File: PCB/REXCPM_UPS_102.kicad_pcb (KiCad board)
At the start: 2 copper layers, 60 x 16 mm, 9 parts, among them J2 SM04B, J3 Conn_02x20_Odd_Even, U1 742G02

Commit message: remove all mention of model 200, since REXCPM does not support it
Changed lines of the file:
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@@
   (paper "USLetter")
   (title_block
-    (title "REXCPM_UPS_102_200")
-    (date "2023-09-14")
-    (rev "002")
+    (title "REXCPM_UPS_102")
+    (date "2023-09-20")
+    (rev "003")
     (company "Brian K. White - b.kenyon.w@gmail.com")
     (comment 1 "github.com/bkw777/REXCPM_UPS")
@@
     (fp_arc (start 4.906989 3.352321) (mid 4.800001 2.952056) (end 4.905239 2.551328)
       (stroke (width 0.1) (type default)) (layer "F.SilkS"))
-    (fp_arc (start 5.3 1.697943) (mid 5.280899 1.852056) (end 5.224755 1.996844)
+    (fp_arc (start 5.3 1.697943) (mid 5.2809 1.852056) (end 5.224755 1.996844)
       (stroke (width 0.1) (type default)) (layer "F.SilkS"))
     (fp_line (start -6.35 -1.6375) (end -5.55 -1.6375)
@@
     (fp_arc (start 4.906989 3.352321) (mid 4.800001 2.952056) (end 4.905239 2.551328)
       (stroke (width 0.1) (type default)) (layer "F.SilkS"))
-    (fp_arc (start 5.3 1.697943) (mid 5.280899 1.852056) (end 5.224755 1.996844)
+    (fp_arc (start 5.3 1.697943) (mid 5.2809 1.852056) (end 5.224755 1.996844)
       (stroke (width 0.1) (type default)) (layer "F.SilkS"))
     (fp_line (start -6.35 -1.6375) (end -5.55 -1.6375)
@@
     (pad "4" smd roundrect (at 1.5 -2) (size 0.6 1.55) (layers "F.Cu" "F.Paste" "F.Mask") (roundrect_rratio 0.25)
       (net 35 "/RAM_RST") (pinfunction "Pin_4") (pintype "passive"))
-    (pad "MP" smd roundrect (at -2.8 1.875) (size 1.2 1.8) (layers "F.Cu" "F.Paste" "F.Mask") (roundrect_rratio 0.208333)
+    (pad "MP" smd roundrect (at -2.8 1.875) (size 1.2 1.8) (layers "F.Cu" "F.Paste" "F.Mask") (roundrect_rratio 0.2083333333)
       (net 1 "GND") (pinfunction "MountPin") (pintype "passive"))
-    (pad "MP" smd roundrect (at 2.8 1.875) (size 1.2 1.8) (layers "F.Cu" "F.Paste" "F.Mask") (roundrect_rratio 0.208333)
+    (pad "MP" smd roundrect (at 2.8 1.875) (size 1.2 1.8) (layers "F.Cu" "F.Paste" "F.Mask") (roundrect_rratio 0.2083333333)
       (net 1 "GND") (pinfunction "MountPin") (pintype "passive"))
     (model "${KIPRJMOD}/000_LOCAL.pretty/000_3d/SM04B-SRSS.step"
@@
     (fp_line (start 5.72 5.1) (end 5.72 -53.36)
       (stroke (width 0.1) (type solid)) (layer "B.Fab"))
-    (pad "1" thru_hole roundrect (at 0 0 270) (size 1.7 1.7) (drill 1) (layers "*.Cu" "*.Mask") (roundrect_rratio 0.147059)
+    (pad "1" thru_hole roundrect (at 0 0 270) (size 1.7 1.7) (drill 1) (layers "*.Cu" "*.Mask") (roundrect_rratio 0.1470588235)
       (net 2 "VBUS") (pinfunction "Pin_1") (pintype "passive"))
     (pad "2" thru_hole circle (at 2.54 0 270) (size 1.7 1.7) (drill 1) (layers "*.Cu" "*.Mask")

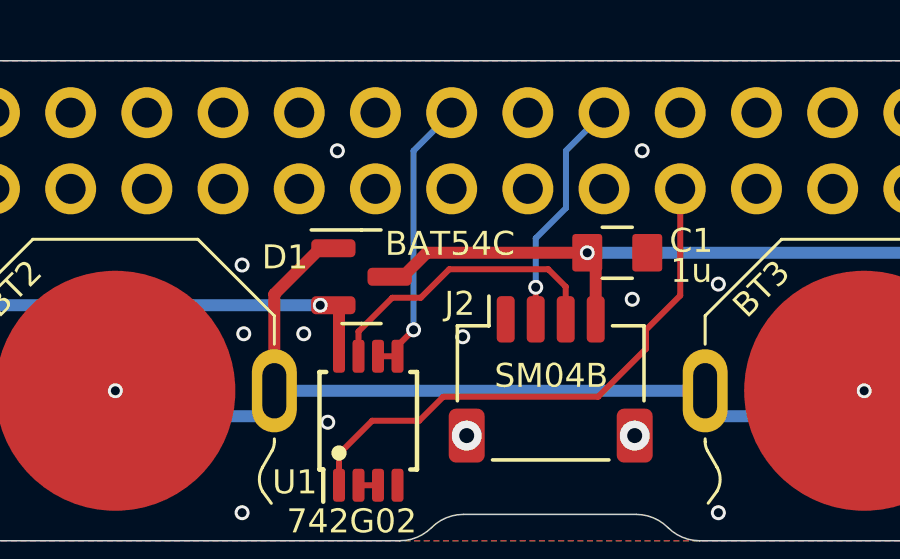
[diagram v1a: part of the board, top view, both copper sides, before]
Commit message: replace BAT54C with BAV170 to protect batteries better
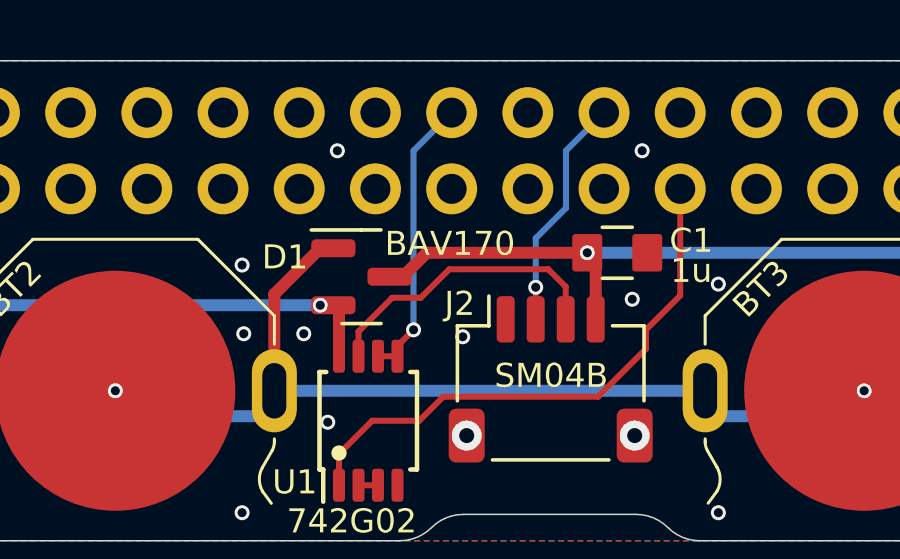
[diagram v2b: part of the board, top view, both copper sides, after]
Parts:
- D1: value BAT54C -> BAV170
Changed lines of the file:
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@@
   (title_block
     (title "REXCPM_UPS_102")
-    (date "2023-09-20")
-    (rev "003")
+    (date "2023-09-21")
+    (rev "004")
     (company "Brian K. White - b.kenyon.w@gmail.com")
     (comment 1 "github.com/bkw777/REXCPM_UPS")
@@
     (descr "SOT, 3 Pin (https://www.jedec.org/system/files/docs/to-236h.pdf variant AB), generated with kicad-footprint-generator ipc_gullwing_generator.py")
     (tags "SOT TO_SOT_SMD")
-    (property "Sheetfile" "REXCPM_UPS_102_200.kicad_sch")
+    (property "Sheetfile" "REXCPM_UPS_102.kicad_sch")
     (property "Sheetname" "")
     (property "ki_description" "dual schottky barrier diode, common cathode")
@@
         (effects (font (size 0.8 0.8) (thickness 0.1)))
     )
-    (fp_text value "BAT54C" (at 2.95 -1.1 unlocked) (layer "F.SilkS")
+    (fp_text value "BAV170" (at 2.95 -1.1 unlocked) (layer "F.SilkS")
         (effects (font (size 0.8 0.8) (thickness 0.1)))
     )
@@
   (footprint "000_LOCAL:Keystone_3031" (layer "F.Cu")
     (at 159.605 112.776)
-    (property "Sheetfile" "REXCPM_UPS_102_200.kicad_sch")
+    (property "Sheetfile" "REXCPM_UPS_102.kicad_sch")
     (property "Sheetname" "")
     (property "ki_description" "Single-cell battery")
@@
     (fp_arc (start 4.906989 3.352321) (mid 4.800001 2.952056) (end 4.905239 2.551328)
       (stroke (width 0.1) (type default)) (layer "F.SilkS"))
-    (fp_arc (start 5.3 1.697943) (mid 5.2809 1.852056) (end 5.224755 1.996844)
+    (fp_arc (start 5.3 1.697943) (mid 5.280899 1.852056) (end 5.224755 1.996844)
       (stroke (width 0.1) (type default)) (layer "F.SilkS"))
     (fp_line (start -6.35 -1.6375) (end -5.55 -1.6375)
@@
   (footprint "000_LOCAL:Keystone_3031" (layer "F.Cu")
     (at 149.005 112.776)
-    (property "Sheetfile" "REXCPM_UPS_102_200.kicad_sch")
+    (property "Sheetfile" "REXCPM_UPS_102.kicad_sch")
     (property "Sheetname" "")
     (property "ki_description" "Single-cell battery")
@@
     (fp_arc (start 4.906989 3.352321) (mid 4.800001 2.952056) (end 4.905239 2.551328)
       (stroke (width 0.1) (type default)) (layer "F.SilkS"))
-    (fp_arc (start 5.3 1.697943) (mid 5.2809 1.852056) (end 5.224755 1.996844)
+    (fp_arc (start 5.3 1.697943) (mid 5.280899 1.852056) (end 5.224755 1.996844)
       (stroke (width 0.1) (type default)) (layer "F.SilkS"))
     (fp_line (start -6.35 -1.6375) (end -5.55 -1.6375)
@@
   (footprint "000_LOCAL:Keystone_3031" (layer "F.Cu")
     (at 124.045 112.776)
-    (property "Sheetfile" "REXCPM_UPS_102_200.kicad_sch")
+    (property "Sheetfile" "REXCPM_UPS_102.kicad_sch")
     (property "Sheetname" "")
     (property "ki_description" "Single-cell battery")
@@
     (descr "TSSOP8: plastic thin shrink small outline package; 8 leads; body width 3 mm; (see NXP SSOP-TSSOP-VSO-REFLOW.pdf and sot505-1_po.pdf)")
     (tags "SSOP 0.65")
-    (property "Sheetfile" "REXCPM_UPS_102_200.kicad_sch")
+    (property "Sheetfile" "REXCPM_UPS_102.kicad_sch")
     (property "Sheetname" "")
     (property "ki_description" "Dual NOR Gate, Low-Voltage CMOS")
@@
     (descr "Capacitor SMD 0805, reflow soldering, AVX (see smccp.pdf)")
     (tags "capacitor 0805")
-    (property "Sheetfile" "REXCPM_UPS_102_200.kicad_sch")
+    (property "Sheetfile" "REXCPM_UPS_102.kicad_sch")
     (property "Sheetname" "")
     (property "ki_description" "Unpolarized capacitor, small symbol")
@@
     (descr "JST SH series connector, SM04B-SRSS-TB (http://www.jst-mfg.com/product/pdf/eng/eSH.pdf), generated with kicad-footprint-generator")
     (tags "connector JST SH top entry")
-    (property "Sheetfile" "REXCPM_UPS_102_200.kicad_sch")
+    (property "Sheetfile" "REXCPM_UPS_102.kicad_sch")
     (property "Sheetname" "")
     (property "ki_description" "Generic connectable mounting pin connector, single row, 01x04, script generated (kicad-library-utils/schlib/autogen/connector/)")
@@
   (footprint "000_LOCAL:Keystone_3031" (layer "F.Cu")
     (at 113.445 112.776)
-    (property "Sheetfile" "REXCPM_UPS_102_200.kicad_sch")
+    (property "Sheetfile" "REXCPM_UPS_102.kicad_sch")
     (property "Sheetname" "")
     (property "ki_description" "Single-cell battery")
@@
     (descr "Through hole IDC box header, 2x20, 2.54mm pitch, DIN 41651 / IEC 60603-13, double rows, https://docs.google.com/spreadsheets/d/16SsEcesNF15N3Lb4niX7dcUr-NY5_MFPQhobNuNppn4/edit#gid=0")
     (tags "Through hole vertical IDC box header THT 2x20 2.54mm double row")
-    (property "Sheetfile" "REXCPM_UPS_102_200.kicad_sch")
+    (property "Sheetfile" "REXCPM_UPS_102.kicad_sch")
     (property "Sheetname" "")
     (property "ki_description" "Generic connector, double row, 02x20, odd/even pin numbering scheme (row 1 odd numbers, row 2 even numbers), script generated (kicad-library-utils/schlib/autogen/connector/)")

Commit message: batt footprint
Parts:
- BT1, BT2, BT3, BT4: value Keystone_3031 -> BAT_3031
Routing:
- net /BATT+: track 67.7 -> 65.9 mm
- net VBUS: track 25.9 -> 25.0 mm
- net GND: vias 27 -> 16
